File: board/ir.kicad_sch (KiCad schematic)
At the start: 7 parts, among them Q3 DMG2302U

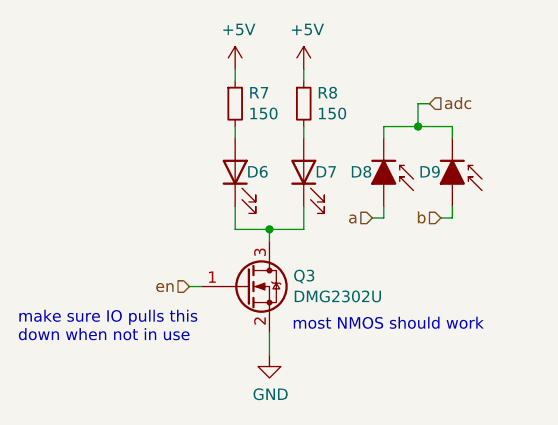
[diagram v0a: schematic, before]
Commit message: Added 3D .step model of Pi Pico and whatever other settings and changes I forgot
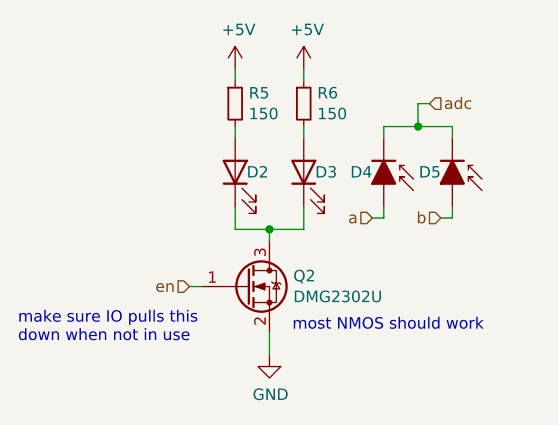
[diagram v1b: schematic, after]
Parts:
- renumbered D6 to D2, D7 to D3, D8 to D4, D9 to D5, Q3 to Q2, R7 to R5, R8 to R6

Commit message: first time running through instantDFM
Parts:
- renumbered D2 to D6, D3 to D7, D4 to D8, D5 to D9, Q2 to Q3, R5 to R7, R6 to R8
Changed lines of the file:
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@@
 (kicad_sch
-	(version 20231120)
+	(version 20250114)
 	(generator "eeschema")
-	(generator_version "8.0")
+	(generator_version "9.0")
 	(paper "A4")
+	(text "make sure IO pulls this\ndown when not in use"
+		(exclude_from_sim no)
+		(at 113.03 119.38 0)
+		(effects
+			(font
+				(size 1.27 1.27)
+			)
+			(justify left bottom)
+		)
+	)
+	(text "most NMOS should work"
+		(exclude_from_sim no)
+		(at 143.51 118.11 0)
+		(effects
+			(font
+				(size 1.27 1.27)
+			)
+			(justify left bottom)
+		)
+	)
 	(junction
 		(at 157.48 95.25)
@@
 		)
 	)
-	(text "make sure IO pulls this\ndown when not in use"
-		(exclude_from_sim no)
-		(at 113.03 119.38 0)
+	(hierarchical_label "b"
+		(shape input)
+		(at 160.02 105.41 180)
 		(effects
 			(font
 				(size 1.27 1.27)
 			)
-			(justify left bottom)
-		)
-	)
-	(text "most NMOS should work"
-		(exclude_from_sim no)
-		(at 143.51 118.11 0)
+			(justify right)
+		)
+	)
+	(hierarchical_label "en"
+		(shape input)
+		(at 132.08 113.03 180)
 		(effects
 			(font
 				(size 1.27 1.27)
 			)
-			(justify left bottom)
-		)
-	)
-	(hierarchical_label "b"
+			(justify right)
+		)
+	)
+	(hierarchical_label "a"
 		(shape input)
-		(at 160.02 105.41 180)
-		(fields_autoplaced yes)
+		(at 152.4 105.41 180)
 		(effects
 			(font
@@
 		)
 	)
-	(hierarchical_label "en"
-		(shape input)
-		(at 132.08 113.03 180)
-		(fields_autoplaced yes)
-		(effects
-			(font
-				(size 1.27 1.27)
-			)
-			(justify right)
-		)
-	)
-	(hierarchical_label "a"
-		(shape input)
-		(at 152.4 105.41 180)
-		(fields_autoplaced yes)
-		(effects
-			(font
-				(size 1.27 1.27)
-			)
-			(justify right)
-		)
-	)
 	(hierarchical_label "adc"
 		(shape input)
 		(at 158.75 92.71 0)
-		(fields_autoplaced yes)
 		(effects
 			(font
@@
 		(on_board yes)
 		(dnp no)
-		(property "Reference" "D5"
+		(property "Reference" "D9"
 			(at 160.02 100.33 90)
 			(effects
@@
 		(on_board yes)
 		(dnp no)
-		(property "Reference" "D4"
+		(property "Reference" "D8"
 			(at 152.4 100.33 90)
 			(effects
@@
 		(on_board yes)
 		(dnp no)
-		(property "Reference" "D2"
+		(property "Reference" "D6"
 			(at 138.43 100.33 90)
 			(effects
@@
 		(on_board yes)
 		(dnp no)
-		(property "Reference" "D3"
+		(property "Reference" "D7"
 			(at 146.05 100.33 90)
 			(effects
@@
 		(on_board yes)
 		(dnp no)
-		(property "Reference" "#PWR026"
+		(property "Reference" "#PWR029"
 			(at 137.16 92.71 0)
 			(effects
@@
 		(on_board yes)
 		(dnp no)
-		(property "Reference" "R5"
+		(property "Reference" "R7"
 			(at 138.6586 91.5416 0)
 			(effects
@@
 		(on_board yes)
 		(dnp no)
-		(property "Reference" "R6"
+		(property "Reference" "R8"
 			(at 146.2786 91.5416 0)
 			(effects
@@
 		(on_board yes)
 		(dnp no)
-		(property "Reference" "Q2"
+		(property "Reference" "Q3"
 			(at 143.6116 111.8616 0)
 			(effects
@@
 		(on_board yes)
 		(dnp no)
-		(property "Reference" "#PWR027"
+		(property "Reference" "#PWR030"
 			(at 140.97 127 0)
 			(effects
@@
 		(on_board yes)
 		(dnp no)
-		(property "Reference" "#PWR028"
+		(property "Reference" "#PWR031"
 			(at 144.78 92.71 0)
 			(effects
